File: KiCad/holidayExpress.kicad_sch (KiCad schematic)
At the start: 23 parts, among them J1 motorPower, J2 motorPower, J3 batteryPower, J4 UARTprogrammer, U1 ESP32-PICO-MINI-02, U2 DRV8833PW, U3 MPM3610GQV-P

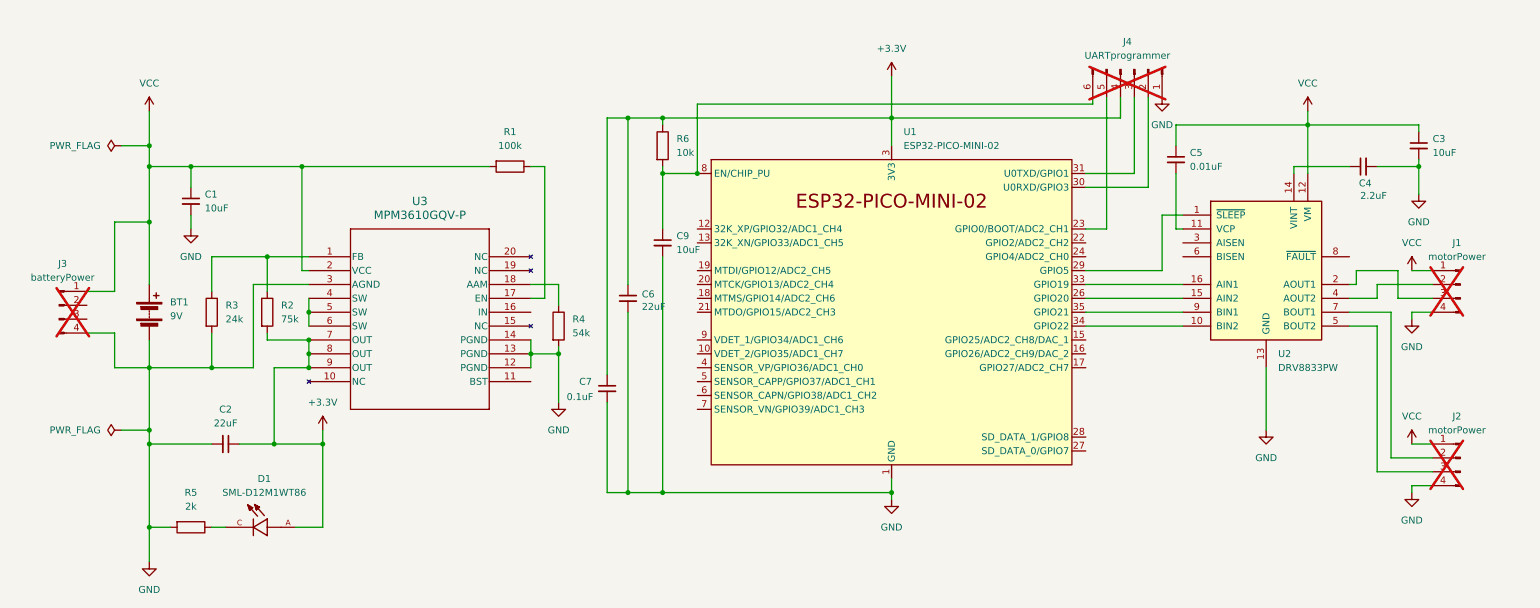
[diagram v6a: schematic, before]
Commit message: correct MPM3610 power input errors
Connect MPM3610 In pin to power, make VCC unconnected. Re-orient UART programmer pins so that direct connection can be used with esp flashy tool. Reorient and optimize PCB layout around MPM changes, add copper pours and larger power traces.
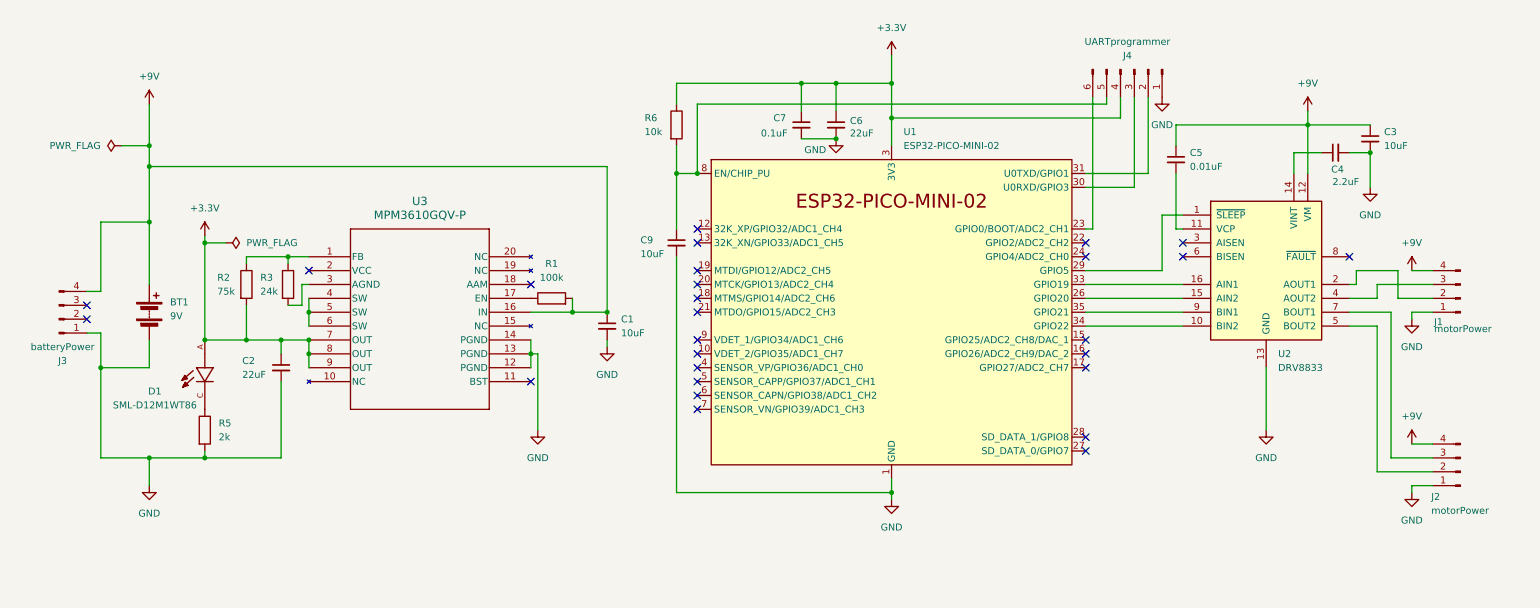
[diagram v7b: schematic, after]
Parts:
- removed R4: 54k, Resistor_SMD:R_0402_1005Metric, symbol Device:R
- J1, J2, J3: footprint Connector_PinHeader_2.54mm:PinHeader_1x04_P2.54mm_Horizontal -> Connector_PinHeader_2.54mm:PinHeader_1x04_P2.54mm_Vertical; now fitted
- J4: footprint Connector_PinHeader_2.54mm:PinHeader_1x06_P2.54mm_Horizontal -> Connector_PinHeader_2.54mm:PinHeader_1x06_P2.54mm_Vertical; now fitted
- U2: value DRV8833PW -> DRV8833; LCSC Part # C50506 -> C154936
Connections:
- net GND: now also J1.1 (Pin_1), J2.1 (Pin_1), J3.1 (Pin_1); no longer J1.4 (Pin_4), J2.4 (Pin_4), J3.4 (Pin_4), R3.2, U3.3 (AGND)
- net at C9.1, R6.2, U1.8 (EN/CHIP_PU): now also J4.5 (Pin_5); no longer J4.6 (Pin_6)
- net at J1.2 (Pin_2): now also U2.2 (AOUT1); no longer U2.4 (AOUT2)
- net at J1.3 (Pin_3): now also U2.4 (AOUT2); no longer U2.2 (AOUT1)
- net at U1.23 (GPIO0/BOOT/ADC2_CH1): now also J4.6 (Pin_6); no longer J4.5 (Pin_5)
- net at J4.2 (Pin_2): now also U1.31 (U0TXD/GPIO1); no longer U1.30 (U0RXD/GPIO3)
- net at J4.3 (Pin_3): now also U1.30 (U0RXD/GPIO3); no longer U1.31 (U0TXD/GPIO1)
- net at J2.2 (Pin_2): now also U2.5 (BOUT2); no longer U2.7 (BOUT1)
- net at J2.3 (Pin_3): now also U2.7 (BOUT1); no longer U2.5 (BOUT2)
- net +9V: now reaches U3.16 (IN)
- net +9V: now also BT1.1 (+), C1.1, C3.1, C5.1, J1.4 (Pin_4), J2.4 (Pin_4), J3.4 (Pin_4), R1.2, U2.12 (VM)
- removed net VCC: BT1.1 (+), C1.1, C3.1, C5.1, J1.1 (Pin_1), J2.1 (Pin_1), J3.1 (Pin_1), R1.2, U2.12 (VM), U3.2 (VCC)
- new net: R3.2, U3.3 (AGND)
- no-connect marks 0 -> 27
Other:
- moved on the sheet: C1, C2, C3, C4, C7, C9, D1, R1, R2, R3, R5, R6

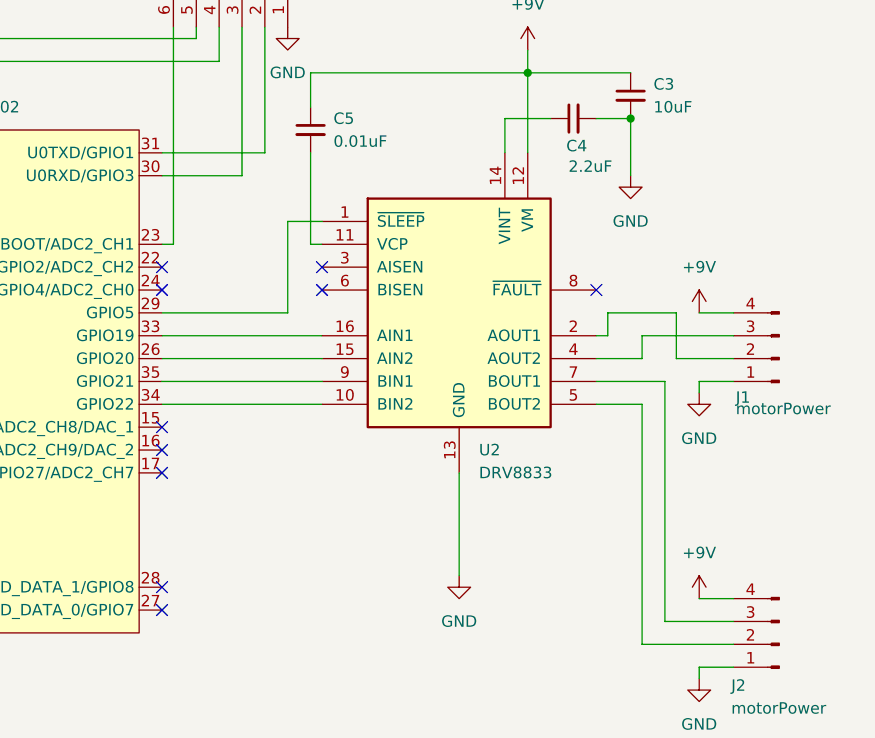
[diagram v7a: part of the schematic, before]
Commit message: fix DRV8833 to use correct symbol
Use QFN symbol so pin mapping matches footprint and part selection.
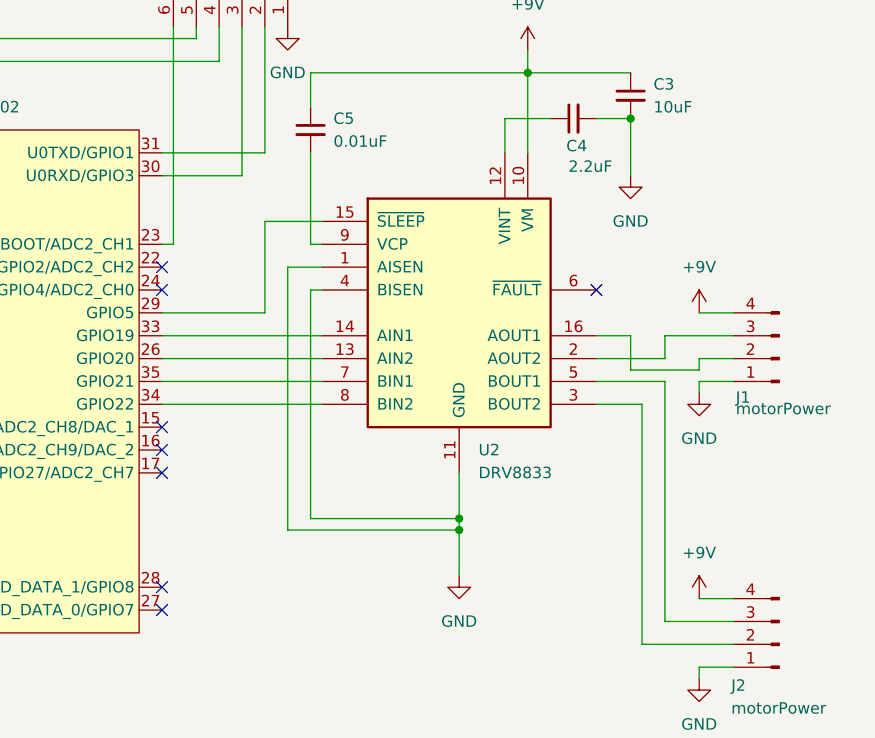
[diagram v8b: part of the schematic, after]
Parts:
- U2: symbol Driver_Motor:DRV8833PW -> Driver_Motor:DRV8833RTY
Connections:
- net +9V: now also U2.10 (VM); no longer U2.12 (VM)
- net GND: now also U2.1 (AISEN), U2.11 (GND), U2.17 (GND), U2.4 (BISEN); no longer U2.13 (GND)
- net at C4.1: now also U2.12 (VINT); no longer U2.14 (VINT)
- net at J2.2 (Pin_2): now also U2.3 (BOUT2); no longer U2.5 (BOUT2)
- net at J2.3 (Pin_3): now also U2.5 (BOUT1); no longer U2.7 (BOUT1)
- net at J1.2 (Pin_2): now also U2.16 (AOUT1); no longer U2.2 (AOUT1)
- net at J1.3 (Pin_3): now also U2.2 (AOUT2); no longer U2.4 (AOUT2)
- net at U1.26 (GPIO20): now also U2.13 (AIN2); no longer U2.15 (AIN2)
- net at U1.29 (GPIO5): now also U2.15 (~{SLEEP}); no longer U2.1 (~{SLEEP})
- net at U1.33 (GPIO19): now also U2.14 (AIN1); no longer U2.16 (AIN1)
- net at U1.34 (GPIO22): now also U2.8 (BIN2); no longer U2.10 (BIN2)
- net at U1.35 (GPIO21): now also U2.7 (BIN1); no longer U2.9 (BIN1)
- net at C5.2: now also U2.9 (VCP); no longer U2.11 (VCP)
- no-connect marks 27 -> 25
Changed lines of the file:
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@@
 (kicad_sch
-	(version 20231120)
+	(version 20250114)
 	(generator "eeschema")
-	(generator_version "8.0")
+	(generator_version "9.0")
 	(paper "A4")
 	(title_block
@@
 	)
 	(junction
+		(at 241.3 85.09)
+		(diameter 0)
+		(color 0 0 0 0)
+	)
+	(junction
 		(at 156.21 26.67)
 		(diameter 0)
@@
 	)
 	(junction
+		(at 241.3 83.82)
+		(diameter 0)
+		(color 0 0 0 0)
+	)
+	(junction
 		(at 172.72 26.67)
 		(diameter 0)
@@
 	)
 	(no_connect
-		(at 226.06 55.88)
-	)
-	(no_connect
 		(at 137.16 63.5)
 	)
@@
 	)
 	(no_connect
-		(at 226.06 58.42)
-	)
-	(no_connect
 		(at 137.16 83.82)
 	)
@@
 	(wire
 		(pts
-			(xy 264.16 95.25) (xy 271.78 95.25)
+			(xy 222.25 85.09) (xy 241.3 85.09)
 		)
 		(stroke
@@
 	(wire
 		(pts
-			(xy 261.62 63.5) (xy 271.78 63.5)
+			(xy 264.16 95.25) (xy 271.78 95.25)
 		)
 		(stroke
@@
 	(wire
 		(pts
+			(xy 267.97 66.04) (xy 271.78 66.04)
+		)
+		(stroke
+			(width 0)
+			(type default)
+		)
+	)
+	(wire
+		(pts
 			(xy 256.54 71.12) (xy 261.62 71.12)
 		)
@@
 	(wire
 		(pts
-			(xy 222.25 50.8) (xy 226.06 50.8)
+			(xy 226.06 55.88) (xy 222.25 55.88)
+		)
+		(stroke
+			(width 0)
+			(type default)
+		)
+	)
+	(wire
+		(pts
+			(xy 219.71 50.8) (xy 226.06 50.8)
 		)
 		(stroke
@@
 	(wire
 		(pts
-			(xy 46.99 55.88) (xy 50.8 55.88)
+			(xy 264.16 63.5) (xy 271.78 63.5)
 		)
 		(stroke
@@
 	(wire
 		(pts
-			(xy 256.54 39.37) (xy 260.35 39.37)
+			(xy 46.99 55.88) (xy 50.8 55.88)
 		)
 		(stroke
@@
 	(wire
 		(pts
-			(xy 261.62 97.79) (xy 271.78 97.79)
+			(xy 256.54 39.37) (xy 260.35 39.37)
 		)
 		(stroke
@@
 	(wire
 		(pts
-			(xy 46.99 54.61) (xy 46.99 55.88)
+			(xy 261.62 97.79) (xy 271.78 97.79)
 		)
 		(stroke
@@
 	(wire
 		(pts
-			(xy 257.81 63.5) (xy 257.81 60.96)
+			(xy 46.99 54.61) (xy 46.99 55.88)
 		)
 		(stroke
@@
 	(wire
 		(pts
+			(xy 224.79 58.42) (xy 226.06 58.42)
+		)
+		(stroke
+			(width 0)
+			(type default)
+		)
+	)
+	(wire
+		(pts
 			(xy 137.16 30.48) (xy 137.16 43.18)
 		)
@@
 	(wire
 		(pts
+			(xy 224.79 83.82) (xy 241.3 83.82)
+		)
+		(stroke
+			(width 0)
+			(type default)
+		)
+	)
+	(wire
+		(pts
 			(xy 36.83 95.25) (xy 36.83 100.33)
 		)
@@
 	(wire
 		(pts
-			(xy 265.43 60.96) (xy 265.43 66.04)
+			(xy 208.28 43.18) (xy 219.71 43.18)
 		)
 		(stroke
@@
 	(wire
 		(pts
-			(xy 208.28 43.18) (xy 219.71 43.18)
+			(xy 62.23 59.69) (xy 62.23 58.42)
 		)
 		(stroke
@@
 	(wire
 		(pts
-			(xy 62.23 59.69) (xy 62.23 58.42)
+			(xy 54.61 73.66) (xy 60.96 73.66)
 		)
 		(stroke
@@
 	(wire
 		(pts
-			(xy 54.61 73.66) (xy 60.96 73.66)
+			(xy 256.54 66.04) (xy 264.16 66.04)
+		)
+		(stroke
+			(width 0)
+			(type default)
+		)
+	)
+	(wire
+		(pts
+			(xy 241.3 83.82) (xy 241.3 85.09)
 		)
 		(stroke
@@
 	(wire
 		(pts
+			(xy 260.35 67.31) (xy 267.97 67.31)
+		)
+		(stroke
+			(width 0)
+			(type default)
+		)
+	)
+	(wire
+		(pts
 			(xy 267.97 92.71) (xy 271.78 92.71)
 		)
@@
 	(wire
 		(pts
-			(xy 208.28 60.96) (xy 222.25 60.96)
+			(xy 208.28 60.96) (xy 219.71 60.96)
 		)
 		(stroke
@@
 	(wire
 		(pts
-			(xy 257.81 60.96) (xy 265.43 60.96)
+			(xy 260.35 63.5) (xy 260.35 67.31)
 		)
 		(stroke
@@
 	(wire
 		(pts
-			(xy 256.54 63.5) (xy 257.81 63.5)
-		)
-		(stroke
-			(width 0)
-			(type default)
-		)
-	)
-	(wire
-		(pts
 			(xy 27.94 78.74) (xy 27.94 95.25)
 		)
@@
 	(wire
 		(pts
-			(xy 256.54 66.04) (xy 261.62 66.04)
+			(xy 36.83 41.91) (xy 120.65 41.91)
 		)
 		(stroke
@@
 	(wire
 		(pts
-			(xy 36.83 41.91) (xy 120.65 41.91)
+			(xy 133.35 43.18) (xy 137.16 43.18)
 		)
 		(stroke
@@
 	(wire
 		(pts
-			(xy 133.35 43.18) (xy 137.16 43.18)
+			(xy 25.4 72.39) (xy 27.94 72.39)
 		)
 		(stroke
@@
 	(wire
 		(pts
-			(xy 25.4 72.39) (xy 27.94 72.39)
+			(xy 25.4 64.77) (xy 27.94 64.77)
 		)
 		(stroke
@@
 	(wire
 		(pts
-			(xy 25.4 64.77) (xy 27.94 64.77)
+			(xy 261.62 71.12) (xy 261.62 97.79)
 		)
 		(stroke
@@
 	(wire
 		(pts
-			(xy 261.62 71.12) (xy 261.62 97.79)
+			(xy 120.65 73.66) (xy 120.65 74.93)
 		)
 		(stroke
@@
 	(wire
 		(pts
-			(xy 120.65 73.66) (xy 120.65 74.93)
+			(xy 267.97 67.31) (xy 267.97 66.04)
 		)
 		(stroke
@@
 	(wire
 		(pts
-			(xy 241.3 78.74) (xy 241.3 90.17)
+			(xy 241.3 78.74) (xy 241.3 83.82)
 		)
 		(stroke
@@
 	(wire
 		(pts
+			(xy 224.79 58.42) (xy 224.79 83.82)
+		)
+		(stroke
+			(width 0)
+			(type default)
+		)
+	)
+	(wire
+		(pts
 			(xy 267.97 101.6) (xy 267.97 100.33)
 		)
@@
 	(wire
 		(pts
+			(xy 241.3 85.09) (xy 241.3 90.17)
+		)
+		(stroke
+			(width 0)
+			(type default)
+		)
+	)
+	(wire
+		(pts
 			(xy 219.71 43.18) (xy 219.71 29.21)
 		)
@@
 	(wire
 		(pts
-			(xy 222.25 60.96) (xy 222.25 50.8)
+			(xy 219.71 60.96) (xy 219.71 50.8)
 		)
 		(stroke
@@
 	(wire
 		(pts
+			(xy 222.25 55.88) (xy 222.25 85.09)
+		)
+		(stroke
+			(width 0)
+			(type default)
+		)
+	)
+	(wire
+		(pts
 			(xy 267.97 68.58) (xy 271.78 68.58)
 		)
@@
 	(wire
 		(pts
-			(xy 265.43 66.04) (xy 271.78 66.04)
+			(xy 256.54 63.5) (xy 260.35 63.5)
 		)
 		(stroke
@@
 	(wire
 		(pts
-			(xy 261.62 66.04) (xy 261.62 63.5)
+			(xy 264.16 66.04) (xy 264.16 63.5)
 		)
 		(stroke
@@
 	)
 	(symbol
-		(lib_id "Driver_Motor:DRV8833PW")
+		(lib_id "Driver_Motor:DRV8833RTY")
 		(at 241.3 60.96 0)
 		(unit 1)
@@
 		(fields_autoplaced yes)
 		(property "Reference" "U2"
-			(at 243.4941 76.2 0)
+			(at 243.4433 76.2 0)
 			(effects
 				(font
@@
 		)
 		(property "Value" "DRV8833"
-			(at 243.4941 78.74 0)
+			(at 243.4433 78.74 0)
 			(effects
 				(font
@@
 			)
 		)
-		(property "Description" "Dual H-Bridge Motor Driver"
+		(property "Description" "Dual H-Bridge Motor Driver, WQFN-16"
 			(at 241.3 60.96 0)
 			(effects
@@
 		(pin "5"
 		)
+		(pin "17"
+		)
 		(instances
 			(project ""
@@
 		)
 	)
+	(embedded_fonts no)
 )
